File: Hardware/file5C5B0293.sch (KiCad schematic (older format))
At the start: 14 parts, among them U12 STM32F030R8Tx

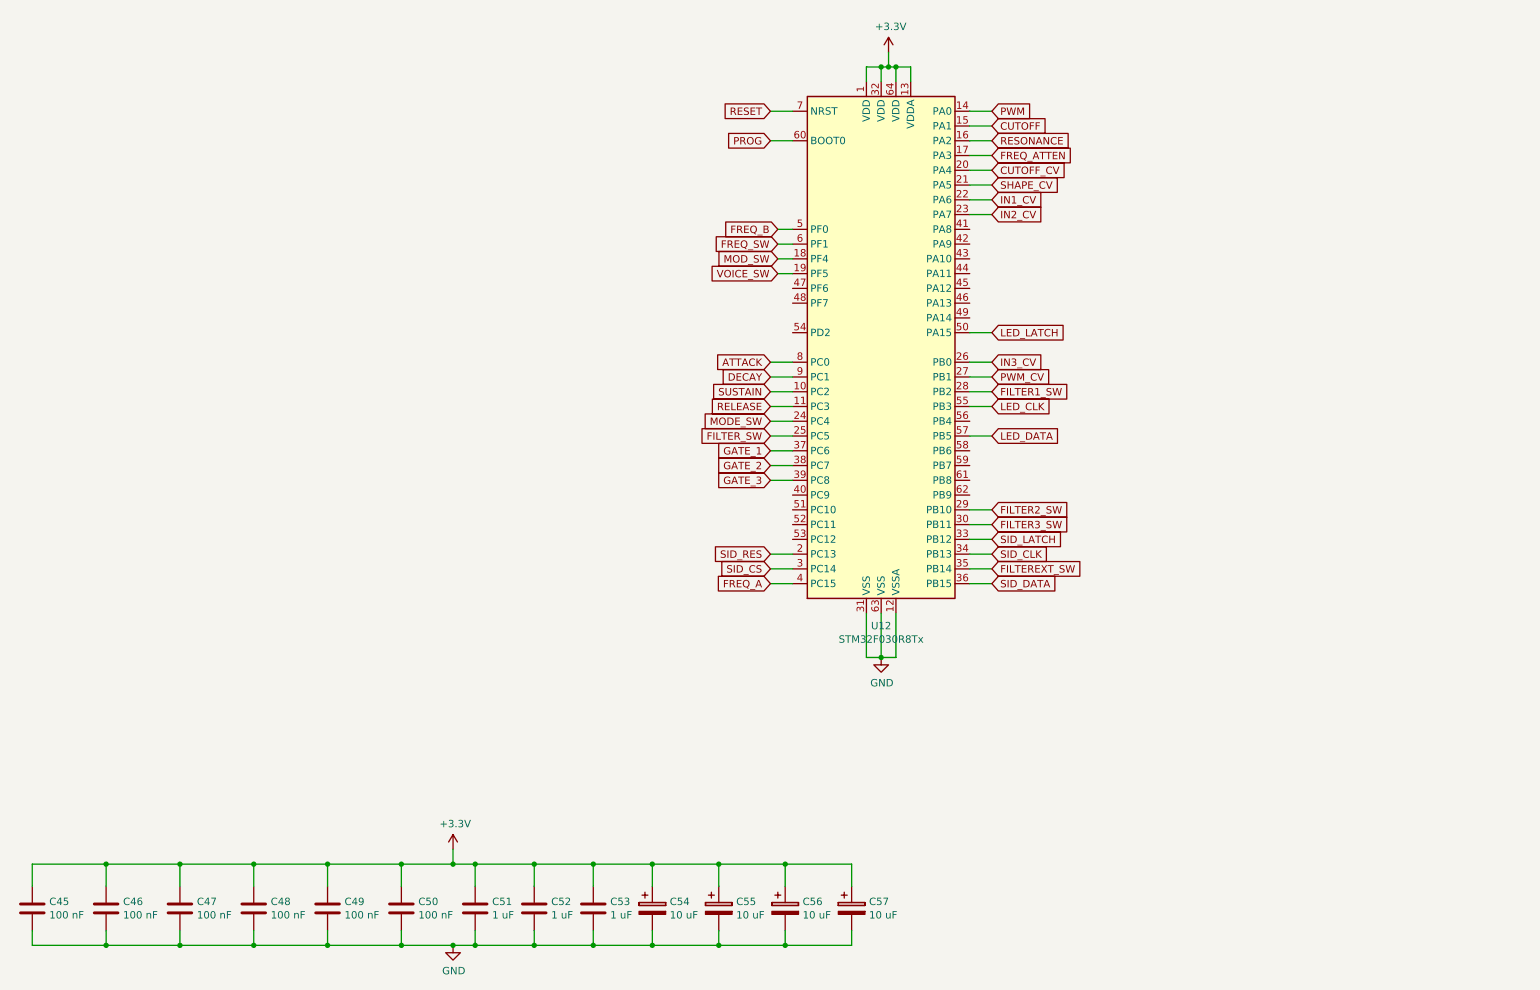
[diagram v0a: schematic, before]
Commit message: Started board layout
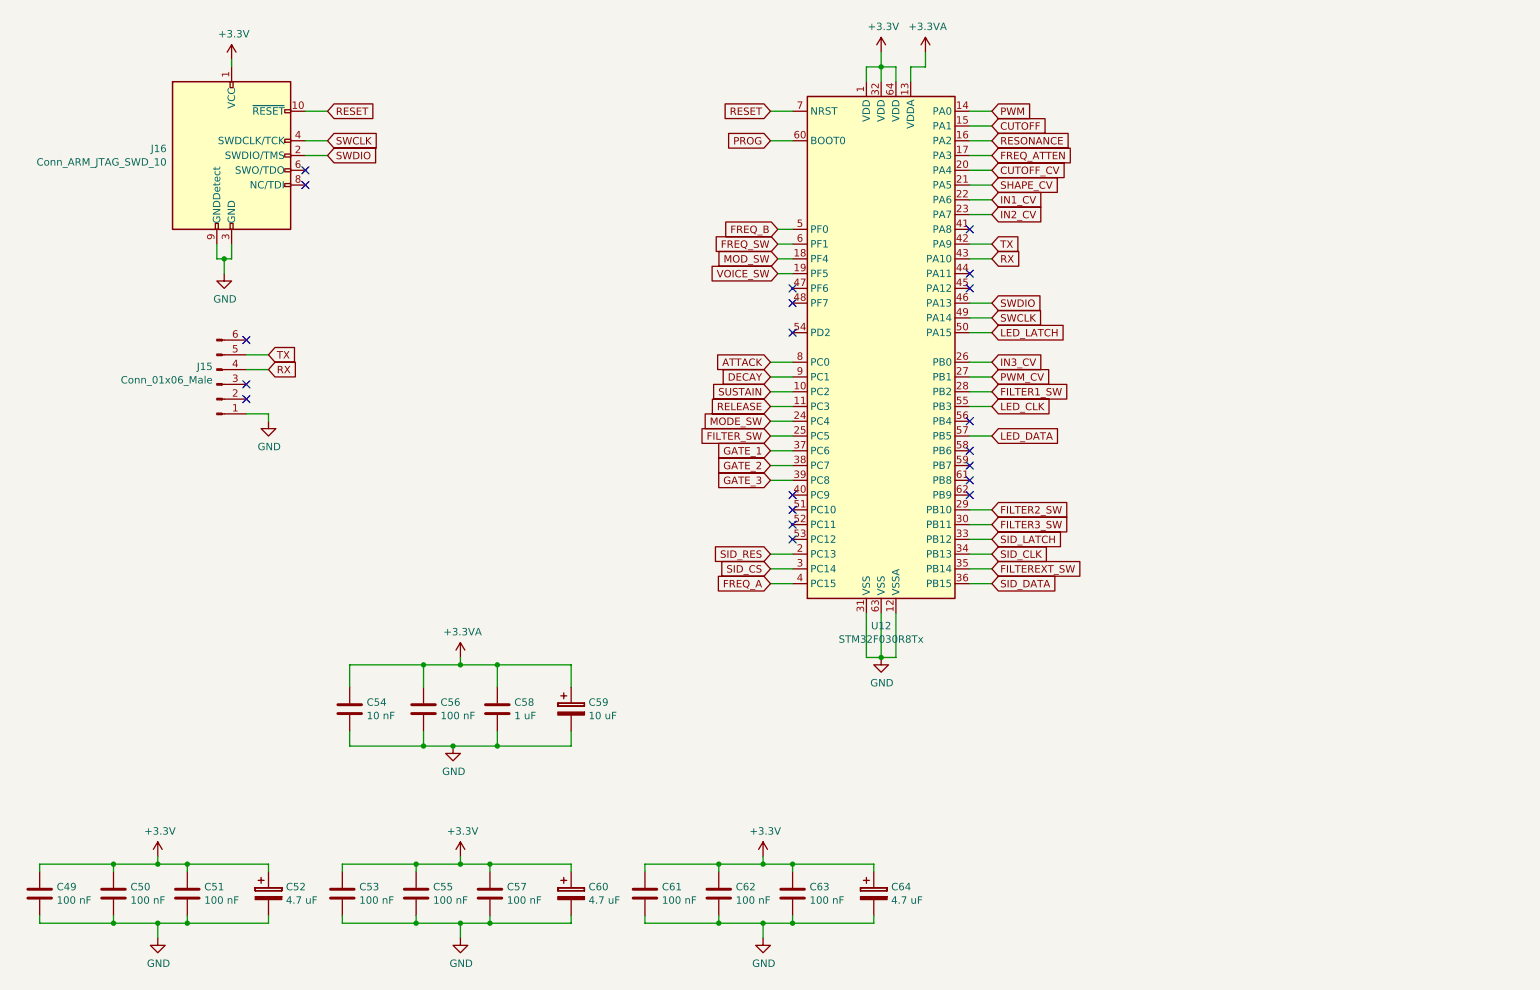
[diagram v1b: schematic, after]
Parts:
- removed C45, C46, C47, C48: 100 nF, symbol Device:C
- removed C52: 1 uF, symbol Device:C
- removed C54, C55, C56, C57: 10 uF, symbol Device:CP
- added C52, C60, C64: 4.7 uF, Capacitors_Tantalum_SMD:CP_Tantalum_Case-A_EIA-3216-18_Reflow, symbol Device:CP
- added C54: 10 nF, Capacitors_SMD:C_0603, symbol Device:C
- added C55, C56, C57, C61, C62, C63: 100 nF, Capacitors_SMD:C_0603, symbol Device:C
- added C58: 1 uF, Capacitors_Tantalum_SMD:CP_Tantalum_Case-R_EIA-2012-12_Reflow, symbol Device:C
- added C59: 10 uF, Capacitors_SMD:CP_Elec_4x5.7, symbol Device:CP
- added J15: Conn_01x06_Male, symbol Connector:Conn_01x06_Male
- added J16: Conn_ARM_JTAG_SWD_10, Connector_PinHeader_1.27mm:PinHeader_2x05_P1.27mm_Vertical_SMD, symbol Connector:Conn_ARM_JTAG_SWD_10
- C49, C50: footprint (none) -> Capacitors_SMD:C_0603
- C51, C53: value 1 uF -> 100 nF; footprint (none) -> Capacitors_SMD:C_0603
- U12: footprint Package_QFP:LQFP-64_10x10mm_P0.5mm -> Housings_QFP:HTQFP-64-1EP_10x10mm_Pitch0.5mm_ThermalPad
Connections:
- net +3V3: now also C52.1, C55.1, C57.1, C60.1, C61.1, C62.1, C63.1, C64.1, J16.1 (VCC); no longer U12.13 (VDDA)
- net GND: now also C52.2, C54.2, C55.2, C56.2, C57.2, C58.2, C59.2, C60.2, C61.2, C62.2, C63.2, C64.2, J15.1 (Pin_1), J16.3 (GND), J16.5 (GND), J16.9 (GNDDetect)
- net RESET: now also J16.10 (~RESET~)
- net TX: now reaches U12.42 (PA9)
- net TX: now also J15.5 (Pin_5)
- net RX: now reaches U12.43 (PA10)
- net RX: now also J15.4 (Pin_4)
- net SWDIO: now reaches U12.46 (PA13)
- net SWDIO: now also J16.2 (SWDIO/TMS)
- net SWCLK: now reaches U12.49 (PA14)
- net SWCLK: now also J16.4 (SWDCLK/TCK)
- new net +3.3VA: C54.1, C56.1, C58.1, C59.1, U12.13 (VDDA)
- no-connect marks 0 -> 20

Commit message: Fixed issues with footprints
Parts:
- C49, C50, C51, C53, C54, C55, C56, C57, C61, C62, C63: footprint Capacitors_SMD:C_0603 -> Capacitor_SMD:C_0603_1608Metric
- C52, C60, C64: footprint Capacitors_Tantalum_SMD:CP_Tantalum_Case-A_EIA-3216-18_Reflow -> Capacitor_Tantalum_SMD:CP_EIA-3216-18_Kemet-A
- C58: footprint Capacitors_Tantalum_SMD:CP_Tantalum_Case-R_EIA-2012-12_Reflow -> Capacitor_Tantalum_SMD:CP_EIA-2012-12_Kemet-R
- C59: footprint Capacitors_SMD:CP_Elec_4x5.7 -> Capacitor_SMD:CP_Elec_4x5.7
- J16: footprint Connector_PinHeader_1.27mm:PinHeader_2x05_P1.27mm_Vertical_SMD -> Connector_PinHeader_1.27mm:PinHeader_2x05_P1.27mm_Vertical
- U12: footprint Housings_QFP:HTQFP-64-1EP_10x10mm_Pitch0.5mm_ThermalPad -> Package_QFP:LQFP-64_10x10mm_P0.5mm
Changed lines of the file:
@@
 F 0 "U12" H 6350 1664 50  0000 C CNN
 F 1 "STM32F030R8Tx" H 6350 1573 50  0000 C CNN
-F 2 "Housings_QFP:HTQFP-64-1EP_10x10mm_Pitch0.5mm_ThermalPad" H 5850 1850 50  0001 R CNN
+F 2 "Package_QFP:LQFP-64_10x10mm_P0.5mm" H 5850 1850 50  0001 R CNN
 F 3 "http://www.st.com/st-web-ui/static/active/en/resource/technical/document/datasheet/DM00088500.pdf" H 6350 3550 50  0001 C CNN
 	1    6350 3550
@@
 F 0 "C56" H 3365 6046 50  0000 L CNN
 F 1 "100 nF" H 3365 5955 50  0000 L CNN
-F 2 "Capacitors_SMD:C_0603" H 3288 5850 50  0001 C CNN
+F 2 "Capacitor_SMD:C_0603_1608Metric" H 3288 5850 50  0001 C CNN
 F 3 "~" H 3250 6000 50  0001 C CNN
 	1    3250 6000
@@
 F 0 "C54" H 2865 6046 50  0000 L CNN
 F 1 "10 nF" H 2865 5955 50  0000 L CNN
-F 2 "Capacitors_SMD:C_0603" H 2788 5850 50  0001 C CNN
+F 2 "Capacitor_SMD:C_0603_1608Metric" H 2788 5850 50  0001 C CNN
 F 3 "~" H 2750 6000 50  0001 C CNN
 	1    2750 6000
@@
 F 0 "C58" H 3865 6046 50  0000 L CNN
 F 1 "1 uF" H 3865 5955 50  0000 L CNN
-F 2 "Capacitors_Tantalum_SMD:CP_Tantalum_Case-R_EIA-2012-12_Reflow" H 3788 5850 50  0001 C CNN
+F 2 "Capacitor_Tantalum_SMD:CP_EIA-2012-12_Kemet-R" H 3788 5850 50  0001 C CNN
 F 3 "~" H 3750 6000 50  0001 C CNN
 	1    3750 6000
@@
 F 0 "C59" H 4368 6046 50  0000 L CNN
 F 1 "10 uF" H 4368 5955 50  0000 L CNN
-F 2 "Capacitors_SMD:CP_Elec_4x5.7" H 4288 5850 50  0001 C CNN
+F 2 "Capacitor_SMD:CP_Elec_4x5.7" H 4288 5850 50  0001 C CNN
 F 3 "~" H 4250 6000 50  0001 C CNN
 	1    4250 6000
@@
 F 0 "C49" H 765 7296 50  0000 L CNN
 F 1 "100 nF" H 765 7205 50  0000 L CNN
-F 2 "Capacitors_SMD:C_0603" H 688 7100 50  0001 C CNN
+F 2 "Capacitor_SMD:C_0603_1608Metric" H 688 7100 50  0001 C CNN
 F 3 "~" H 650 7250 50  0001 C CNN
 	1    650  7250
@@
 F 0 "C50" H 1265 7296 50  0000 L CNN
 F 1 "100 nF" H 1265 7205 50  0000 L CNN
-F 2 "Capacitors_SMD:C_0603" H 1188 7100 50  0001 C CNN
+F 2 "Capacitor_SMD:C_0603_1608Metric" H 1188 7100 50  0001 C CNN
 F 3 "~" H 1150 7250 50  0001 C CNN
 	1    1150 7250
@@
 F 0 "C51" H 1765 7296 50  0000 L CNN
 F 1 "100 nF" H 1765 7205 50  0000 L CNN
-F 2 "Capacitors_SMD:C_0603" H 1688 7100 50  0001 C CNN
+F 2 "Capacitor_SMD:C_0603_1608Metric" H 1688 7100 50  0001 C CNN
 F 3 "~" H 1650 7250 50  0001 C CNN
 	1    1650 7250
@@
 F 0 "C52" H 2318 7296 50  0000 L CNN
 F 1 "4.7 uF" H 2318 7205 50  0000 L CNN
-F 2 "Capacitors_Tantalum_SMD:CP_Tantalum_Case-A_EIA-3216-18_Reflow" H 2238 7100 50  0001 C CNN
+F 2 "Capacitor_Tantalum_SMD:CP_EIA-3216-18_Kemet-A" H 2238 7100 50  0001 C CNN
 F 3 "~" H 2200 7250 50  0001 C CNN
 	1    2200 7250
@@
 F 0 "C53" H 2815 7296 50  0000 L CNN
 F 1 "100 nF" H 2815 7205 50  0000 L CNN
-F 2 "Capacitors_SMD:C_0603" H 2738 7100 50  0001 C CNN
+F 2 "Capacitor_SMD:C_0603_1608Metric" H 2738 7100 50  0001 C CNN
 F 3 "~" H 2700 7250 50  0001 C CNN
 	1    2700 7250
@@
 F 0 "C55" H 3315 7296 50  0000 L CNN
 F 1 "100 nF" H 3315 7205 50  0000 L CNN
-F 2 "Capacitors_SMD:C_0603" H 3238 7100 50  0001 C CNN
+F 2 "Capacitor_SMD:C_0603_1608Metric" H 3238 7100 50  0001 C CNN
 F 3 "~" H 3200 7250 50  0001 C CNN
 	1    3200 7250
@@
 F 0 "C57" H 3815 7296 50  0000 L CNN
 F 1 "100 nF" H 3815 7205 50  0000 L CNN
-F 2 "Capacitors_SMD:C_0603" H 3738 7100 50  0001 C CNN
+F 2 "Capacitor_SMD:C_0603_1608Metric" H 3738 7100 50  0001 C CNN
 F 3 "~" H 3700 7250 50  0001 C CNN
 	1    3700 7250
@@
 F 0 "C60" H 4368 7296 50  0000 L CNN
 F 1 "4.7 uF" H 4368 7205 50  0000 L CNN
-F 2 "Capacitors_Tantalum_SMD:CP_Tantalum_Case-A_EIA-3216-18_Reflow" H 4288 7100 50  0001 C CNN
+F 2 "Capacitor_Tantalum_SMD:CP_EIA-3216-18_Kemet-A" H 4288 7100 50  0001 C CNN
 F 3 "~" H 4250 7250 50  0001 C CNN
 	1    4250 7250
@@
 F 0 "C61" H 4865 7296 50  0000 L CNN
 F 1 "100 nF" H 4865 7205 50  0000 L CNN
-F 2 "Capacitors_SMD:C_0603" H 4788 7100 50  0001 C CNN
+F 2 "Capacitor_SMD:C_0603_1608Metric" H 4788 7100 50  0001 C CNN
 F 3 "~" H 4750 7250 50  0001 C CNN
 	1    4750 7250
@@
 F 0 "C62" H 5365 7296 50  0000 L CNN
 F 1 "100 nF" H 5365 7205 50  0000 L CNN
-F 2 "Capacitors_SMD:C_0603" H 5288 7100 50  0001 C CNN
+F 2 "Capacitor_SMD:C_0603_1608Metric" H 5288 7100 50  0001 C CNN
 F 3 "~" H 5250 7250 50  0001 C CNN
 	1    5250 7250
@@
 F 0 "C63" H 5865 7296 50  0000 L CNN
 F 1 "100 nF" H 5865 7205 50  0000 L CNN
-F 2 "Capacitors_SMD:C_0603" H 5788 7100 50  0001 C CNN
+F 2 "Capacitor_SMD:C_0603_1608Metric" H 5788 7100 50  0001 C CNN
 F 3 "~" H 5750 7250 50  0001 C CNN
 	1    5750 7250
@@
 F 0 "C64" H 6418 7296 50  0000 L CNN
 F 1 "4.7 uF" H 6418 7205 50  0000 L CNN
-F 2 "Capacitors_Tantalum_SMD:CP_Tantalum_Case-A_EIA-3216-18_Reflow" H 6338 7100 50  0001 C CNN
+F 2 "Capacitor_Tantalum_SMD:CP_EIA-3216-18_Kemet-A" H 6338 7100 50  0001 C CNN
 F 3 "~" H 6300 7250 50  0001 C CNN
 	1    6300 7250
@@
 F 0 "J16" H 1510 2296 50  0000 R CNN
 F 1 "Conn_ARM_JTAG_SWD_10" H 1510 2205 50  0000 R CNN
-F 2 "Connector_PinHeader_1.27mm:PinHeader_2x05_P1.27mm_Vertical_SMD" H 2000 1700 50  0001 L TNN
+F 2 "Connector_PinHeader_1.27mm:PinHeader_2x05_P1.27mm_Vertical" H 2000 1700 50  0001 L TNN
 F 3 "http://infocenter.arm.com/help/topic/com.arm.doc.faqs/attached/13634/cortex_debug_connectors.pdf" V 1600 1000 50  0001 C CNN
 	1    1950 2250

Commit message: Finished assigning footprints
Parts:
- J15: footprint (none) -> Connector_PinHeader_2.54mm:PinHeader_1x06_P2.54mm_Vertical
- J16: footprint Connector_PinHeader_1.27mm:PinHeader_2x05_P1.27mm_Vertical -> Connector_PinHeader_2.54mm:PinHeader_2x05_P2.54mm_Vertical
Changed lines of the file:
@@
 F 0 "J16" H 1510 2296 50  0000 R CNN
 F 1 "Conn_ARM_JTAG_SWD_10" H 1510 2205 50  0000 R CNN
-F 2 "Connector_PinHeader_1.27mm:PinHeader_2x05_P1.27mm_Vertical" H 2000 1700 50  0001 L TNN
+F 2 "Connector_PinHeader_2.54mm:PinHeader_2x05_P2.54mm_Vertical" H 2000 1700 50  0001 L TNN
 F 3 "http://infocenter.arm.com/help/topic/com.arm.doc.faqs/attached/13634/cortex_debug_connectors.pdf" V 1600 1000 50  0001 C CNN
 	1    1950 2250
@@
 F 0 "J15" H 1822 3680 50  0000 R CNN
 F 1 "Conn_01x06_Male" H 1822 3771 50  0000 R CNN
-F 2 "" H 1850 3800 50  0001 C CNN
+F 2 "Connector_PinHeader_2.54mm:PinHeader_1x06_P2.54mm_Vertical" H 1850 3800 50  0001 C CNN
 F 3 "~" H 1850 3800 50  0001 C CNN
 	1    1850 3800
